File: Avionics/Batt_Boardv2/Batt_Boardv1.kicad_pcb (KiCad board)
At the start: 2 copper layers, 90.2 x 95.9 mm, 30 parts, among them J1 Conn_02x26_Odd_Even, J2 Conn_02x26_Odd_Even, Q1 IRF7458, Q2 IRF7458, U3 TMP36xS

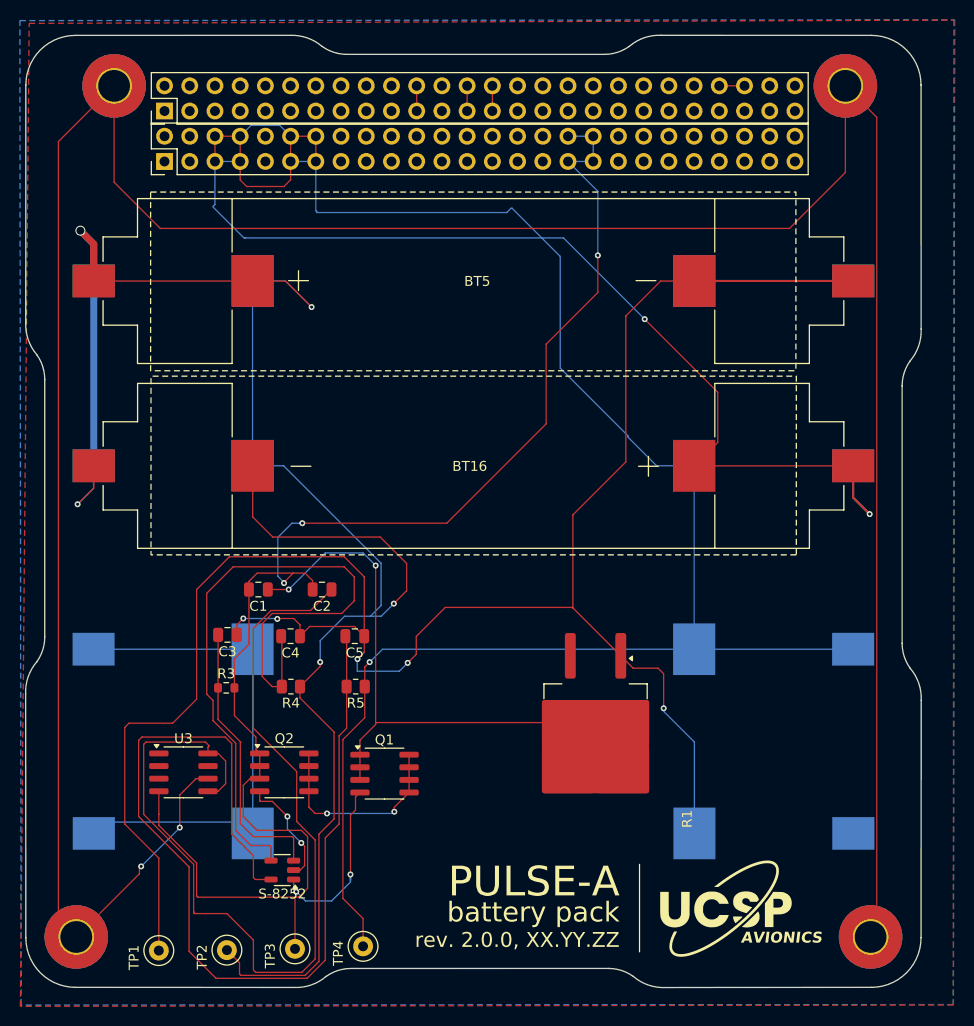
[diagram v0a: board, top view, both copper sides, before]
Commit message: 12/17/2024, Sephora Poteau: Replaced power traces with filled zones
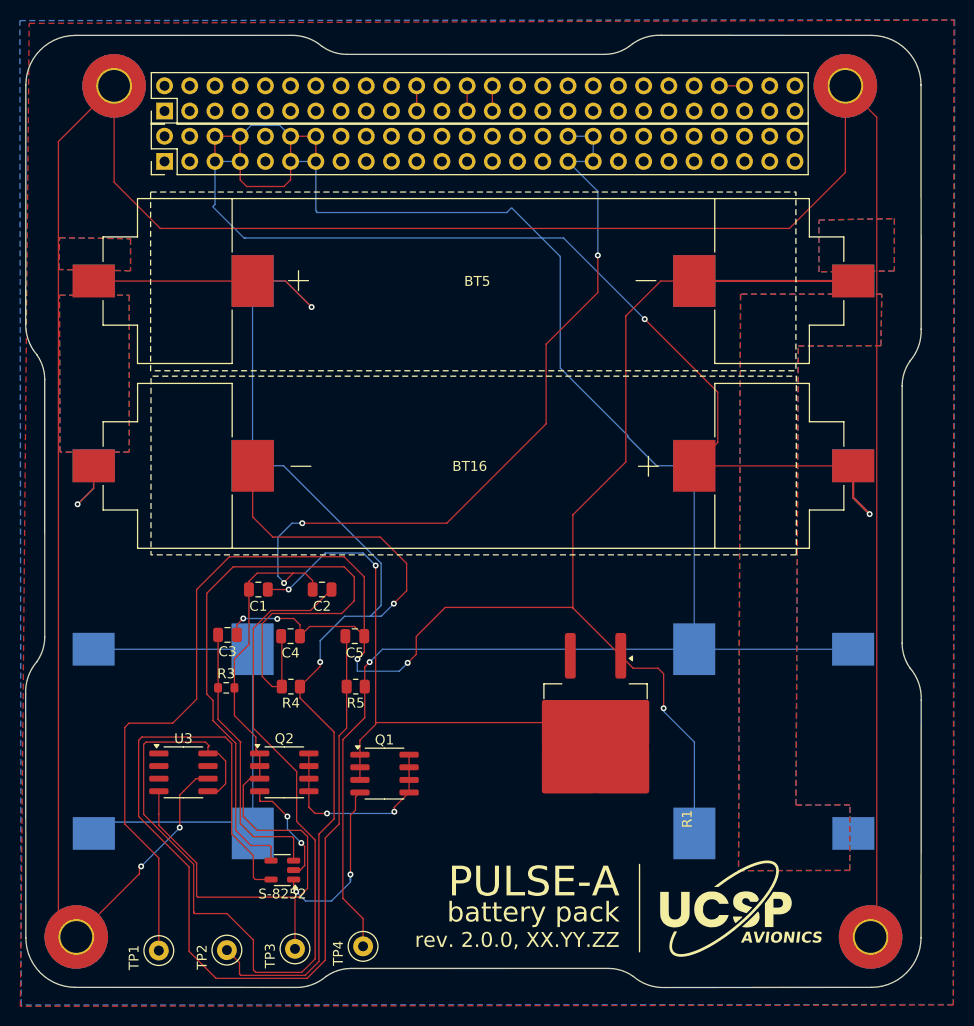
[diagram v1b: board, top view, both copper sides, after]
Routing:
- net /BM: track 193.4 -> 163.5 mm, vias 5 -> 4
- added copper zone on B.Cu, net /B-
- added copper zone on F.Cu, net /B-
- added copper zone on B.Cu, net /BATT_PRE_INH
- added copper zone on F.Cu, net /BATT_PRE_INH
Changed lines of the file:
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@@
-	)
-	(segment
-		(start 106.471377 70.657377)
-		(end 106.471377 74.39075)
-		(width 0.7)
-		(layer "F.Cu")
-		(net 13)
 	)
 	(segment
@@
 		(end 129.286 113.207868)
 		(width 0.1)
-		(layer "F.Cu")
-		(net 13)
-	)
-	(segment
-		(start 105.1306 69.3166)
-		(end 106.471377 70.657377)
-		(width 0.7)
 		(layer "F.Cu")
 		(net 13)
@@
 		(net 13)
 	)
-	(via
-		(at 105.1306 69.3166)
-		(size 1)
-		(drill 0.8)
-		(layers "F.Cu" "B.Cu")
-		(net 13)
-	)
 	(segment
 		(start 106.48016 92.971696)
@@
 	)
 	(segment
-		(start 106.48016 70.66616)
-		(end 105.1306 69.3166)
-		(width 0.7)
-		(layer "B.Cu")
-		(net 13)
-	)
-	(segment
 		(start 135.4328 108.1532)
 		(end 134.3406 108.1532)
@@
 	)
 	(segment
-		(start 106.48016 74.376)
-		(end 106.48016 70.66616)
-		(width 0.7)
-		(layer "B.Cu")
-		(net 13)
-	)
-	(segment
 		(start 125.7856 74.376)
 		(end 128.4224 77.0128)
 		(width 0.1)
-		(layer "B.Cu")
-		(net 13)
-	)
-	(segment
-		(start 106.48016 74.376)
-		(end 106.48016 92.971696)
-		(width 0.7)
 		(layer "B.Cu")
 		(net 13)
@@
 			)
 		)
+	)
+	(zone
+		(net 8)
+		(net_name "/B-")
+		(layers "F&B.Cu")
+		(name "B-")
+		(hatch edge 0.5)
+		(priority 2)
+		(connect_pads
+			(clearance 0.254)
+		)
+		(min_thickness 0.25)
+		(filled_areas_thickness no)
+		(fill yes
+			(thermal_gap 0.5)
+			(thermal_bridge_width 0.5)
+			(island_removal_mode 1)
+			(island_area_min 10)
+		)
+		(polygon
+			(pts
+				(xy 179.5272 73.4568) (xy 179.5272 68.2498) (xy 187.1218 68.0974) (xy 187.1218 73.3806)
+			)
+		)
+	)
+	(zone
+		(net 6)
+		(net_name "/BATT_PRE_INH")
+		(layers "F&B.Cu")
+		(name "BPI")
+		(hatch edge 0.5)
+		(priority 5)
+		(connect_pads
+			(clearance 0.254)
+		)
+		(min_thickness 0.25)
+		(filled_areas_thickness no)
+		(fill yes
+			(thermal_gap 0.5)
+			(thermal_bridge_width 0.5)
+		)
+		(polygon
+			(pts
+				(xy 103.0224 75.819) (xy 110.0582 75.819) (xy 110.0582 91.6178) (xy 103.0732 91.6178)
+			)
+		)
+	)
+	(zone
+		(net 8)
+		(net_name "/B-")
+		(layers "F&B.Cu")
+		(name "B-")
+		(hatch edge 0.5)
+		(priority 3)
+		(connect_pads
+			(clearance 0.254)
+		)
+		(min_thickness 0.25)
+		(filled_areas_thickness no)
+		(fill yes
+			(thermal_gap 0.5)
+			(thermal_bridge_width 0.5)
+			(island_removal_mode 1)
+			(island_area_min 10)
+		)
+		(polygon
+			(pts
+				(xy 171.6278 75.7174) (xy 171.4246 133.7818) (xy 182.626 133.7564) (xy 182.6514 127.1524) (xy 177.2158 127.1778)
+				(xy 177.4444 80.9244) (xy 185.7756 80.899) (xy 185.8518 75.7174)
+			)
+		)
+	)
+	(zone
+		(net 6)
+		(net_name "/BATT_PRE_INH")
+		(layers "F&B.Cu")
+		(name "BPI")
+		(hatch edge 0.5)
+		(priority 4)
+		(connect_pads
+			(clearance 0.254)
+		)
+		(min_thickness 0.25)
+		(filled_areas_thickness no)
+		(fill yes
+			(thermal_gap 0.5)
+			(thermal_bridge_width 0.5)
+			(island_removal_mode 1)
+			(island_area_min 10)
+		)
+		(polygon
+			(pts
+				(xy 103.0224 70.0278) (xy 110.1852 70.1294) (xy 110.1852 73.3552) (xy 102.9716 73.2282)
+			)
+		)

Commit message: 12/18/2024, Sephora Poteau: Added power planes to Batt_Boardv2 and increased clearance by 1mm
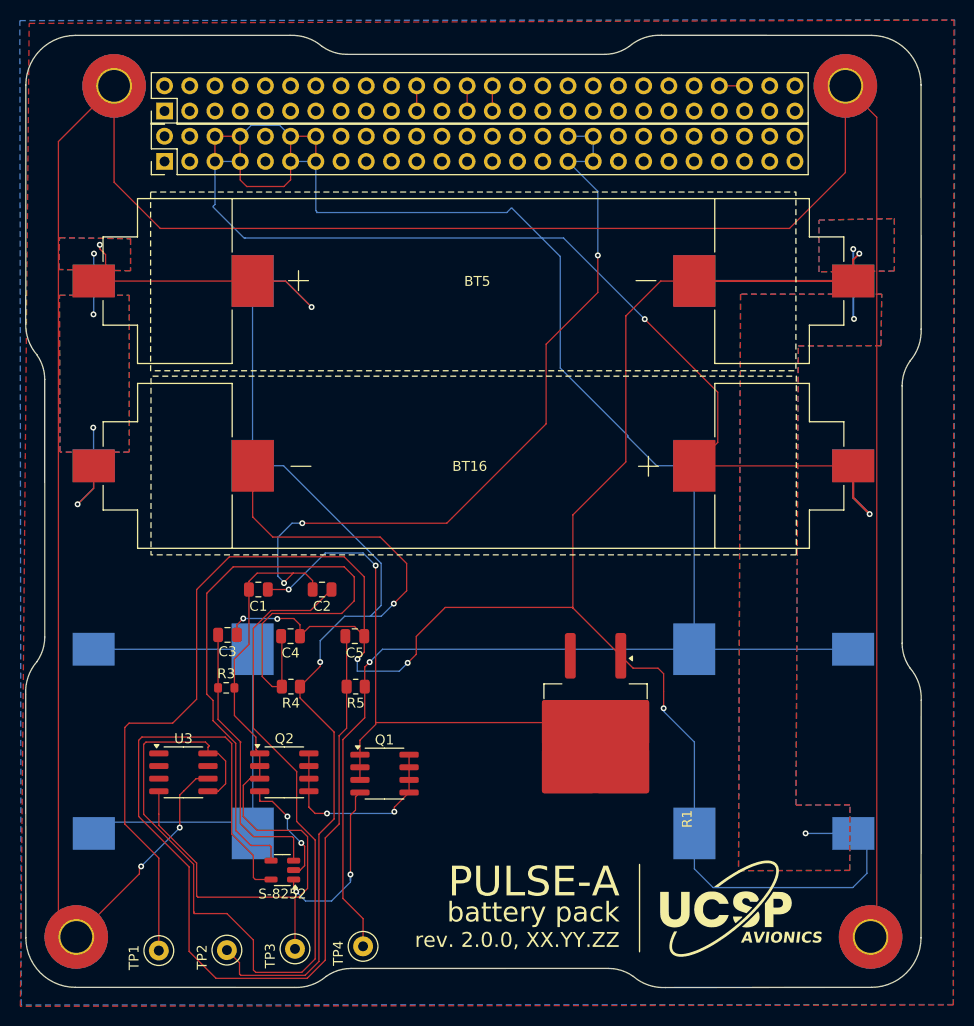
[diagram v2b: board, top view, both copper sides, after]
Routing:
- net /B-: track 216.6 -> 258.4 mm, vias 5 -> 9
- net /BM: track 163.5 -> 177.9 mm, vias 4 -> 8
- added copper zone on B.Cu, net /BM
- added copper zone on F.Cu, net /BM
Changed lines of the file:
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@@
+	)
+	(segment
+		(start 182.974223 72.244977)
+		(end 183.5912 71.628)
+		(width 0.2)
+		(layer "F.Cu")
+		(net 8)
 	)
 	(segment
@@
 	)
 	(segment
+		(start 182.974223 74.39075)
+		(end 182.974223 72.244977)
+		(width 0.2)
+		(layer "F.Cu")
+		(net 8)
+	)
+	(segment
 		(start 109.603334 119.3546)
 		(end 110.0324 118.925534)
@@
 	)
 	(via
+		(at 182.9816 71.1708)
+		(size 0.6)
+		(drill 0.3)
+		(layers "F.Cu" "B.Cu")
+		(net 8)
+	)
+	(via
 		(at 121.541334 108.379201)
 		(size 0.6)
@@
 	)
 	(via
+		(at 183.5912 71.628)
+		(size 0.6)
+		(drill 0.3)
+		(layers "F.Cu" "B.Cu")
+		(net 8)
+	)
+	(via
+		(at 183.0578 78.2066)
+		(size 0.6)
+		(drill 0.3)
+		(layers "F.Cu" "B.Cu")
+		(net 8)
+	)
+	(via
+		(at 178.181 130.0226)
+		(size 0.6)
+		(drill 0.3)
+		(layers "F.Cu" "B.Cu")
+		(net 8)
+	)
+	(via
 		(at 163.883134 117.426934)
 		(size 0.6)
 		(drill 0.3)
 		(layers "F.Cu" "B.Cu")
+		(net 8)
+	)
+	(segment
+		(start 168.8592 135.4836)
+		(end 166.979121 133.603521)
+		(width 0.1)
+		(layer "B.Cu")
 		(net 8)
 	)
@@
 	)
 	(segment
+		(start 182.983006 71.172206)
+		(end 182.9816 71.1708)
+		(width 0.2)
+		(layer "B.Cu")
+		(net 8)
+	)
+	(segment
 		(start 166.973006 74.376)
 		(end 182.983006 74.376)
@@
 	)
 	(segment
+		(start 184.3532 131.395942)
+		(end 184.3532 134.0612)
+		(width 0.1)
+		(layer "B.Cu")
+		(net 8)
+	)
+	(segment
 		(start 133.0198 113.6904)
 		(end 133.0198 112.4966)
@@
 	)
 	(segment
+		(start 182.983006 78.131806)
+		(end 183.0578 78.2066)
+		(width 0.2)
+		(layer "B.Cu")
+		(net 8)
+	)
+	(segment
 		(start 182.989121 130.031863)
 		(end 182.989121 129.054947)
@@
 	)
 	(segment
+		(start 182.989121 130.031863)
+		(end 178.190263 130.031863)
+		(width 0.1)
+		(layer "B.Cu")
+		(net 8)
+	)
+	(segment
 		(start 163.883134 117.731734)
 		(end 166.979121 120.827721)
@@
 	)
 	(segment
+		(start 182.989121 130.031863)
+		(end 184.3532 131.395942)
+		(width 0.1)
+		(layer "B.Cu")
+		(net 8)
+	)
+	(segment
+		(start 182.9308 135.4836)
+		(end 168.8592 135.4836)
+		(width 0.1)
+		(layer "B.Cu")
+		(net 8)
+	)
+	(segment
+		(start 166.979121 133.603521)
+		(end 166.979121 130.031863)
+		(width 0.1)
+		(layer "B.Cu")
+		(net 8)
+	)
+	(segment
 		(start 121.546667 108.384534)
 		(end 121.541334 108.379201)
@@
 	)
 	(segment
+		(start 182.983006 74.376)
+		(end 182.983006 78.131806)
+		(width 0.2)
+		(layer "B.Cu")
+		(net 8)
+	)
+	(segment
+		(start 182.983006 74.376)
+		(end 182.983006 71.172206)
+		(width 0.2)
+		(layer "B.Cu")
+		(net 8)
+	)
+	(segment
 		(start 137.2616 113.6904)
 		(end 133.0198 113.6904)
@@
 	)
 	(segment
+		(start 178.190263 130.031863)
+		(end 178.181 130.0226)
+		(width 0.1)
+		(layer "B.Cu")
+		(net 8)
+	)
+	(segment
+		(start 184.3532 134.0612)
+		(end 182.9308 135.4836)
+		(width 0.1)
+		(layer "B.Cu")
+		(net 8)
+	)
+	(segment
 		(start 138.240334 123.370534)
 		(end 138.240334 125.910534)
@@
 	)
 	(segment
+		(start 107.6706 71.7296)
+		(end 107.0864 71.1454)
+		(width 0.1)
+		(layer "F.Cu")
+		(net 13)
+	)
+	(segment
+		(start 107.6706 73.191527)
+		(end 107.6706 71.7296)
+		(width 0.1)
+		(layer "F.Cu")
+		(net 13)
+	)
+	(segment
 		(start 125.80035 74.39075)
 		(end 122.481377 74.39075)
@@
 	)
 	(segment
+		(start 106.471377 74.39075)
+		(end 107.6706 73.191527)
+		(width 0.1)
+		(layer "F.Cu")
+		(net 13)
+	)
+	(segment
 		(start 129.161334 142.928534)
 		(end 127.764334 144.325534)
@@
 	)
 	(segment
+		(start 107.0864 71.1454)
+		(end 107.0864 70.739)
+		(width 0.1)
+		(layer "F.Cu")
+		(net 13)
+	)
+	(segment
 		(start 137.9982 102.8446)
 		(end 137.9982 105.5878)
@@
 	)
 	(via
+		(at 106.5022 71.628)
+		(size 0.6)
+		(drill 0.3)
+		(layers "F.Cu" "B.Cu")
+		(net 13)
+	)
+	(via
+		(at 106.4514 77.7494)
+		(size 0.6)
+		(drill 0.3)
+		(layers "F.Cu" "B.Cu")
+		(net 13)
+	)
+	(via
 		(at 129.286 112.776)
 		(size 0.6)
@@
 	)
 	(via
+		(at 106.426 89.154)
+		(size 0.6)
+		(drill 0.3)
+		(layers "F.Cu" "B.Cu")
+		(net 13)
+	)
+	(via
 		(at 104.8512 96.8756)
 		(size 0.6)
@@
 	(via
 		(at 136.7028 106.8832)
+		(size 0.6)
+		(drill 0.3)
+		(layers "F.Cu" "B.Cu")
+		(net 13)
+	)
+	(via
+		(at 107.0864 70.739)
 		(size 0.6)
 		(drill 0.3)
@@
 	)
 	(segment
+		(start 106.48016 71.65004)
+		(end 106.5022 71.628)
+		(width 0.1)
+		(layer "B.Cu")
+		(net 13)
+	)
+	(segment
 		(start 135.426334 107.067466)
 		(end 134.3406 108.1532)
@@
 	)
 	(segment
+		(start 106.461146 92.99071)
+		(end 106.461146 89.189146)
+		(width 0.1)
+		(layer "B.Cu")
+		(net 13)
+	)
+	(segment
 		(start 136.7028 106.8832)
 		(end 135.4328 108.1532)
@@
 	)
 	(segment
+		(start 106.461146 89.189146)
+		(end 106.426 89.154)
+		(width 0.1)
+		(layer "B.Cu")
+		(net 13)
+	)
+	(segment
 		(start 131.7498 108.1532)
 		(end 129.286 110.617)
@@
 	)
 	(segment
+		(start 106.48016 74.376)
+		(end 106.48016 71.65004)
+		(width 0.1)
+		(layer "B.Cu")
+		(net 13)
+	)
+	(segment
 		(start 106.461146 95.265654)
 		(end 106.461146 92.99071)
@@
 	)
 	(segment
+		(start 106.48016 74.376)
+		(end 106.48016 77.72064)
+		(width 0.1)
+		(layer "B.Cu")
+		(net 13)
+	)
+	(segment
 		(start 129.286 110.617)
 		(end 129.286 112.776)
@@
 		(start 122.471146 92.99071)
 		(end 125.594328 92.99071)
+		(width 0.1)
+		(layer "B.Cu")
+		(net 13)
+	)
+	(segment
+		(start 106.48016 77.72064)
+		(end 106.4514 77.7494)
 		(width 0.1)
 		(layer "B.Cu")
@@
 	)
 	(zone
-		(net 6)
-		(net_name "/BATT_PRE_INH")
+		(net 13)
+		(net_name "/BM")
 		(layers "F&B.Cu")
 		(name "BPI")

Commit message: PDU 3.0.0
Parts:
- BT16: moved to B.Cu
- BT4: moved to F.Cu
- moved BT2 38.5 mm to (144.8, 131.4)
- moved BT4 36.7 mm to (144.8, 93.3)
- moved BT16 19.3 mm to (144.8, 112.4)
- moved BT1 18.1 mm to (144.8, 93.3)
- moved BT5 0.33 mm to (144.8, 74.3)
- moved BT3 0.33 mm to (144.8, 74.3)
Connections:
- BT1 pad 2: Net-(BT1-BATT-) -> /BM
- BT4 pad 1: Net-(BT1-BATT-) -> /BM
- H1 pad 1: GNDREF -> (no net)
- H2 pad 1: GNDREF -> (no net)
- H3 pad 1: GNDREF -> (no net)
- H4 pad 1: GNDREF -> (no net)
- U3 pad 6: GNDREF -> (no net)
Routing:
- net GNDREF: track 446.5 -> 0.00 mm, vias 5 -> 0
- net /BATT_PRE_INH: track 293.5 -> 0.00 mm, vias 3 -> 0
- net /B-: track 258.4 -> 0.00 mm, vias 9 -> 0
- net /BM: track 177.9 -> 0.00 mm, vias 8 -> 0
- net /VDD: track 98.6 -> 0.00 mm
- net /3V3: track 95.8 -> 0.00 mm
- net Net-(S-8252-VC): track 72.6 -> 0.00 mm
- net Net-(C1-Pad1): track 69.9 -> 0.00 mm, vias 2 -> 0
- net Net-(BT1-BATT-): track 51.5 -> 0.00 mm
- net Net-(S-8252-V-): track 28.2 -> 0.00 mm
- net Net-(Q1-D-Pad5): track 20.7 -> 0.00 mm, vias 2 -> 0
- net Net-(Q1-G): track 18.1 -> 0.00 mm, vias 2 -> 1
- net Net-(Q2-G): track 11.4 -> 0.00 mm, vias 2 -> 0
- net V_BATT: track 2.54 -> 0.00 mm
- net /EDFA_5V_SW: track 2.54 -> 0.00 mm
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- removed copper zone on F.Cu, net /BATT_PRE_INH
- removed copper zone on B.Cu, net GNDREF
- removed copper zone on F.Cu, net GNDREF
